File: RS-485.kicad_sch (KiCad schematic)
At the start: 15 parts, among them IC1 MAX485ESA+T

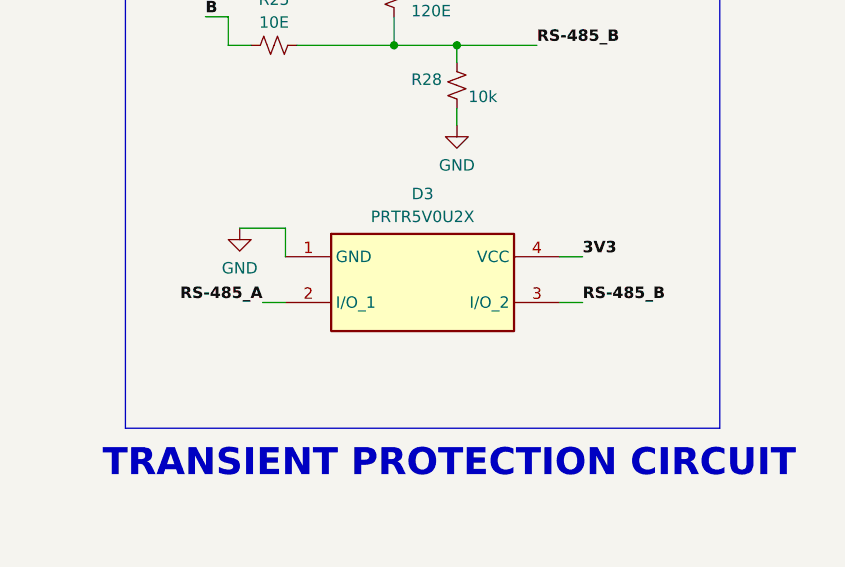
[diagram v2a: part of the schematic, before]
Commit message: Added IP5306 for power path management
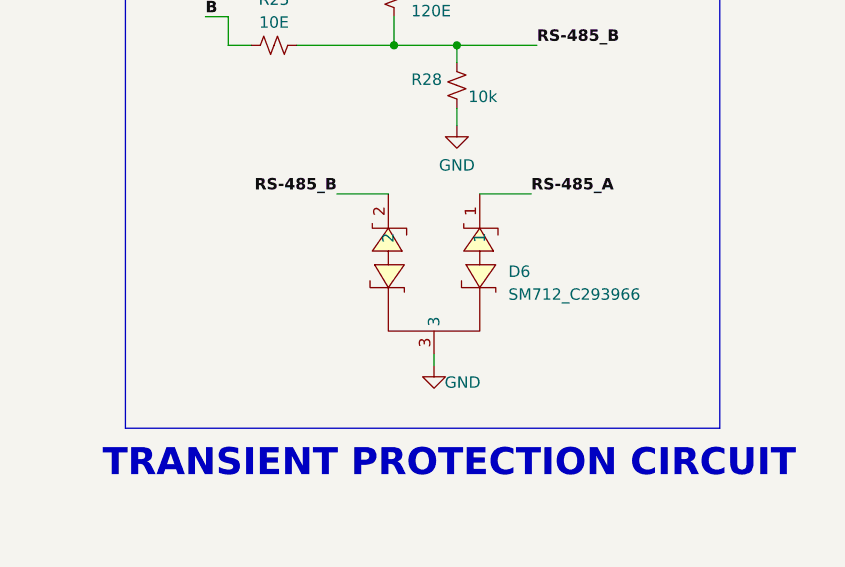
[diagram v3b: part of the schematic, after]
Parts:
- removed D3: PRTR5V0U2X, PRTR5V0U2X, symbol ESP32-S3_DB:PRTR5V0U2X
- added D6: SM712_C293966, easyeda2kicad:SOT-23_L2.9-W1.3-P1.90-LS2.4-BR, symbol ESP32-S3_DB:SM712_C293966
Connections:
- net GND: now also D6.3
- net RS_485_A: now also D6.1
- net RS_485_B: now also D6.2
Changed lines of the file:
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@@
+    (stroke (width 0) (type default))
+  )
+  (wire (pts (xy 234.95 106.68) (xy 229.235 106.68))
     (stroke (width 0) (type default))
   )
@@
     (stroke (width 0) (type default))
   )
-  (wire (pts (xy 256.54 113.665) (xy 254 113.665))
-    (stroke (width 0) (type default))
-  )
   (wire (pts (xy 125.095 108.585) (xy 125.095 111.76))
     (stroke (width 0) (type default))
@@
     (stroke (width 0) (type default))
   )
-  (wire (pts (xy 223.52 110.49) (xy 223.52 113.665))
-    (stroke (width 0) (type default))
-  )
   (wire (pts (xy 217.17 83.185) (xy 217.17 80.01))
     (stroke (width 0) (type default))
@@
     (stroke (width 0) (type default))
   )
-  (wire (pts (xy 220.98 118.745) (xy 223.52 118.745))
-    (stroke (width 0) (type default))
-  )
   (wire (pts (xy 62.865 102.235) (xy 60.96 102.235))
     (stroke (width 0) (type default))
@@
     (stroke (width 0) (type default))
   )
+  (wire (pts (xy 240.03 125.73) (xy 240.03 124.46))
+    (stroke (width 0) (type default))
+  )
   (wire (pts (xy 41.275 110.49) (xy 46.99 110.49))
     (stroke (width 0) (type default))
@@
     (stroke (width 0) (type default))
   )
-  (wire (pts (xy 218.44 110.49) (xy 223.52 110.49))
-    (stroke (width 0) (type default))
-  )
   (wire (pts (xy 235.585 86.995) (xy 235.585 90.17))
     (stroke (width 0) (type default))
@@
     (stroke (width 1) (type default) (color 72 72 72 1))
   )
-  (wire (pts (xy 256.54 118.745) (xy 254 118.745))
-    (stroke (width 0) (type default))
-  )
   (wire (pts (xy 235.585 90.17) (xy 242.57 90.17))
     (stroke (width 0) (type default))
@@
   )
   (wire (pts (xy 47.625 186.69) (xy 33.655 186.69))
+    (stroke (width 0) (type default))
+  )
+  (wire (pts (xy 250.825 106.68) (xy 245.11 106.68))
     (stroke (width 0) (type default))
   )
@@
     (effects (font (size 1.27 1.27) (thickness 0.254) bold (color 0 0 255 1)) (justify right bottom))
   )
-  (label "RS-485_A" (at 220.98 118.745 180) (fields_autoplaced)
-    (effects (font (size 1.27 1.27) (thickness 0.254) bold (color 0 0 0 1)) (justify right bottom))
+  (label "RS-485_A" (at 250.825 106.68 0) (fields_autoplaced)
+    (effects (font (size 1.27 1.27) (thickness 0.254) bold (color 0 0 0 1)) (justify left bottom))
   )
   (label "3V3" (at 47.625 165.735 180) (fields_autoplaced)
     (effects (font (size 1.27 1.27) (thickness 0.254) bold (color 255 0 0 1)) (justify right bottom))
   )
-  (label "3V3" (at 256.54 113.665 0) (fields_autoplaced)
-    (effects (font (size 1.27 1.27) (thickness 0.254) bold (color 255 0 0 1)) (justify left bottom))
-  )
   (label "RS-485_A" (at 47.625 181.61 180) (fields_autoplaced)
     (effects (font (size 1.27 1.27) (thickness 0.254) bold (color 0 0 0 1)) (justify right bottom))
@@
     (effects (font (size 1.27 1.27) (thickness 0.254) bold (color 0 0 255 1)) (justify right bottom))
   )
-  (label "RS-485_B" (at 256.54 118.745 0) (fields_autoplaced)
-    (effects (font (size 1.27 1.27) (thickness 0.254) bold (color 0 0 0 1)) (justify left bottom))
+  (label "RS-485_B" (at 229.235 106.68 180) (fields_autoplaced)
+    (effects (font (size 1.27 1.27) (thickness 0.254) bold (color 0 0 0 1)) (justify right bottom))
   )
   (hierarchical_label "485_TX" (shape output) (at 33.655 170.815 180) (fields_autoplaced)
@@
     )
   )
-  (symbol (lib_id "ESP32-S3_DB:PRTR5V0U2X") (at 223.52 113.665 0) (unit 1)
-    (in_bom yes) (on_board yes) (dnp no) (fields_autoplaced)
-    (property "Reference" "D3" (at 238.76 106.68 0)
-      (effects (font (size 1.27 1.27)))
-    )
-    (property "Value" "PRTR5V0U2X" (at 238.76 109.22 0)
-      (effects (font (size 1.27 1.27)))
-    )
-    (property "Footprint" "PRTR5V0U2X" (at 250.19 208.585 0)
-      (effects (font (size 1.27 1.27)) (justify left top) hide)
-    )
-    (property "Datasheet" "https://assets.nexperia.com/documents/data-sheet/PRTR5V0U2X.pdf" (at 250.19 308.585 0)
-      (effects (font (size 1.27 1.27)) (justify left top) hide)
-    )
-    (property "Height" "1.1" (at 250.19 508.585 0)
-      (effects (font (size 1.27 1.27)) (justify left top) hide)
-    )
-    (property "Manufacturer_Name" "Nexperia" (at 250.19 608.585 0)
-      (effects (font (size 1.27 1.27)) (justify left top) hide)
-    )
-    (property "Manufacturer_Part_Number" "PRTR5V0U2X" (at 250.19 708.585 0)
-      (effects (font (size 1.27 1.27)) (justify left top) hide)
-    )
-    (property "Mouser Part Number" "N/A" (at 250.19 808.585 0)
-      (effects (font (size 1.27 1.27)) (justify left top) hide)
-    )
-    (property "Mouser Price/Stock" "https://www.mouser.co.uk/ProductDetail/Nexperia/PRTR5V0U2X?qs=vHuUswq2%252BsxqVTVM0kNyWw%3D%3D" (at 250.19 908.585 0)
-      (effects (font (size 1.27 1.27)) (justify left top) hide)
-    )
-    (property "Arrow Part Number" "" (at 250.19 1008.585 0)
-      (effects (font (size 1.27 1.27)) (justify left top) hide)
-    )
-    (property "Arrow Price/Stock" "" (at 250.19 1108.585 0)
-      (effects (font (size 1.27 1.27)) (justify left top) hide)
-    )
-    (pin "1")
-    (pin "2")
-    (pin "3")
-    (pin "4")
-    (instances
-      (project "ESP32-S3_DB"
-        (path "/b7fc4bd3-c219-4455-832b-8d795385dcf1/9b4afe2f-79e5-4a56-98d7-d16b193c0e70"
-          (reference "D3") (unit 1)
-        )
-      )
-    )
-  )
   (symbol (lib_id "ESP32-S3_DB:R_Small_US") (at 222.25 90.17 90) (unit 1)
     (in_bom yes) (on_board yes) (dnp no) (fields_autoplaced)
@@
     )
   )
-  (symbol (lib_id "ESP32-S3_DB:GND") (at 218.44 110.49 0) (unit 1)
+  (symbol (lib_id "ESP32-S3_DB:GND") (at 240.03 125.73 0) (unit 1)
+    (in_bom yes) (on_board yes) (dnp no)
+    (property "Reference" "#PWR037" (at 240.03 132.08 0)
+      (effects (font (size 1.27 1.27)) hide)
+    )
+    (property "Value" "GND" (at 243.205 127.635 0)
+      (effects (font (size 1.27 1.27)))
+    )
+    (property "Footprint" "" (at 240.03 125.73 0)
+      (effects (font (size 1.27 1.27)) hide)
+    )
+    (property "Datasheet" "" (at 240.03 125.73 0)
+      (effects (font (size 1.27 1.27)) hide)
+    )
+    (pin "1")
+    (instances
+      (project "ESP32-S3_DB"
+        (path "/b7fc4bd3-c219-4455-832b-8d795385dcf1/9b4afe2f-79e5-4a56-98d7-d16b193c0e70"
+          (reference "#PWR037") (unit 1)
+        )
+      )
+    )
+  )
+  (symbol (lib_id "ESP32-S3_DB:SM712_C293966") (at 240.03 114.3 180) (unit 1)
     (in_bom yes) (on_board yes) (dnp no) (fields_autoplaced)
-    (property "Reference" "#PWR037" (at 218.44 116.84 0)
-      (effects (font (size 1.27 1.27)) hide)
-    )
-    (property "Value" "GND" (at 218.44 114.935 0)
-      (effects (font (size 1.27 1.27)))
-    )
-    (property "Footprint" "" (at 218.44 110.49 0)
-      (effects (font (size 1.27 1.27)) hide)
-    )
-    (property "Datasheet" "" (at 218.44 110.49 0)
-      (effects (font (size 1.27 1.27)) hide)
-    )
-    (pin "1")
-    (instances
-      (project "ESP32-S3_DB"
-        (path "/b7fc4bd3-c219-4455-832b-8d795385dcf1/9b4afe2f-79e5-4a56-98d7-d16b193c0e70"
-          (reference "#PWR037") (unit 1)
-        )
-      )
+    (property "Reference" "D6" (at 248.285 115.315 0)
+      (effects (font (size 1.27 1.27)) (justify right))
+    )
+    (property "Value" "SM712_C293966" (at 248.285 117.855 0)
+      (effects (font (size 1.27 1.27)) (justify right))
+    )
+    (property "Footprint" "easyeda2kicad:SOT-23_L2.9-W1.3-P1.90-LS2.4-BR" (at 240.03 99.06 0)
+      (effects (font (size 1.27 1.27)) hide)
+    )
+    (property "Datasheet" "https://lcsc.com/product-detail/TVS_DOWO-SM712_C293966.html" (at 240.03 96.52 0)
+      (effects (font (size 1.27 1.27)) hide)
+    )
+    (property "LCSC Part" "C293966" (at 240.03 93.98 0)
+      (effects (font (size 1.27 1.27)) hide)
+    )
+    (pin "1")
+    (pin "2")
+    (pin "3")
+    (instances
+      (project "ESP32-S3_DB"
+        (path "/b7fc4bd3-c219-4455-832b-8d795385dcf1/9b4afe2f-79e5-4a56-98d7-d16b193c0e70"
+          (reference "D6") (unit 1)
+        )
+      )

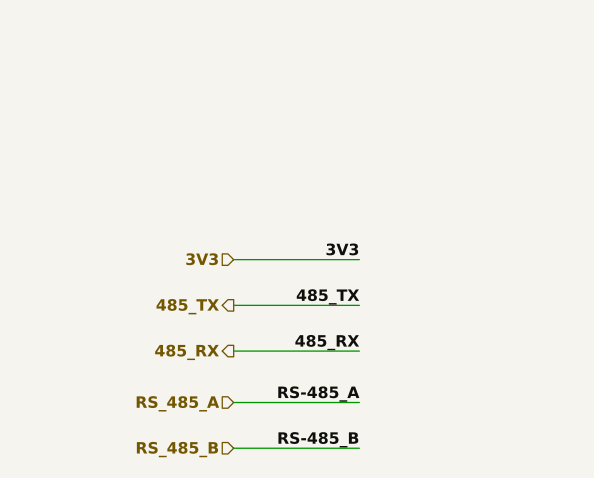
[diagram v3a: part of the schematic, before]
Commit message: Assigned UART port 2 for RS-485
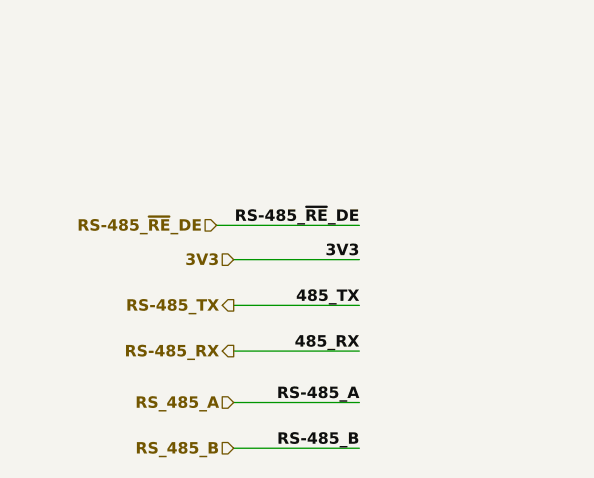
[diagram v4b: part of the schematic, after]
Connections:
- net 485_RX renamed RS-485_RX
- net 485_TX renamed RS-485_TX
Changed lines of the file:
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@@
+    (stroke (width 0) (type default))
+  )
+  (wire (pts (xy 47.625 161.925) (xy 31.75 161.925))
     (stroke (width 0) (type default))
   )
@@
   )
   (label "RS-485_~{RE}_DE" (at 110.49 96.52 0) (fields_autoplaced)
-    (effects (font (size 1.27 1.27) bold (color 0 132 132 1)) (justify left bottom))
+    (effects (font (size 1.27 1.27) bold (color 0 194 0 1)) (justify left bottom))
   )
   (label "B" (at 214.63 86.995 0) (fields_autoplaced)
@@
     (effects (font (size 1.27 1.27) (thickness 0.254) bold (color 0 0 0 1)) (justify right bottom))
   )
+  (label "RS-485_~{RE}_DE" (at 47.625 161.925 180) (fields_autoplaced)
+    (effects (font (size 1.27 1.27) bold (color 0 194 0 1)) (justify right bottom))
+  )
   (label "3V3" (at 247.015 71.12 180) (fields_autoplaced)
     (effects (font (size 1.27 1.27) (thickness 0.254) bold (color 255 0 0 1)) (justify right bottom))
@@
     (effects (font (size 1.27 1.27) (thickness 0.254) bold (color 0 0 0 1)) (justify right bottom))
   )
-  (hierarchical_label "485_TX" (shape output) (at 33.655 170.815 180) (fields_autoplaced)
+  (hierarchical_label "RS-485_TX" (shape output) (at 33.655 170.815 180) (fields_autoplaced)
     (effects (font (size 1.27 1.27) bold (color 0 0 255 1)) (justify right))
   )
@@
     (effects (font (size 1.27 1.27) (thickness 0.254) bold (color 255 0 0 1)) (justify right))
   )
-  (hierarchical_label "485_RX" (shape output) (at 33.655 175.895 180) (fields_autoplaced)
+  (hierarchical_label "RS-485_RX" (shape output) (at 33.655 175.895 180) (fields_autoplaced)
     (effects (font (size 1.27 1.27) bold (color 0 0 255 1)) (justify right))
   )
+  (hierarchical_label "RS-485_~{RE}_DE" (shape input) (at 31.75 161.925 180) (fields_autoplaced)
+    (effects (font (size 1.27 1.27) bold (color 0 194 0 1)) (justify right))
+  )
   (hierarchical_label "RS_485_B" (shape input) (at 33.655 186.69 180) (fields_autoplaced)

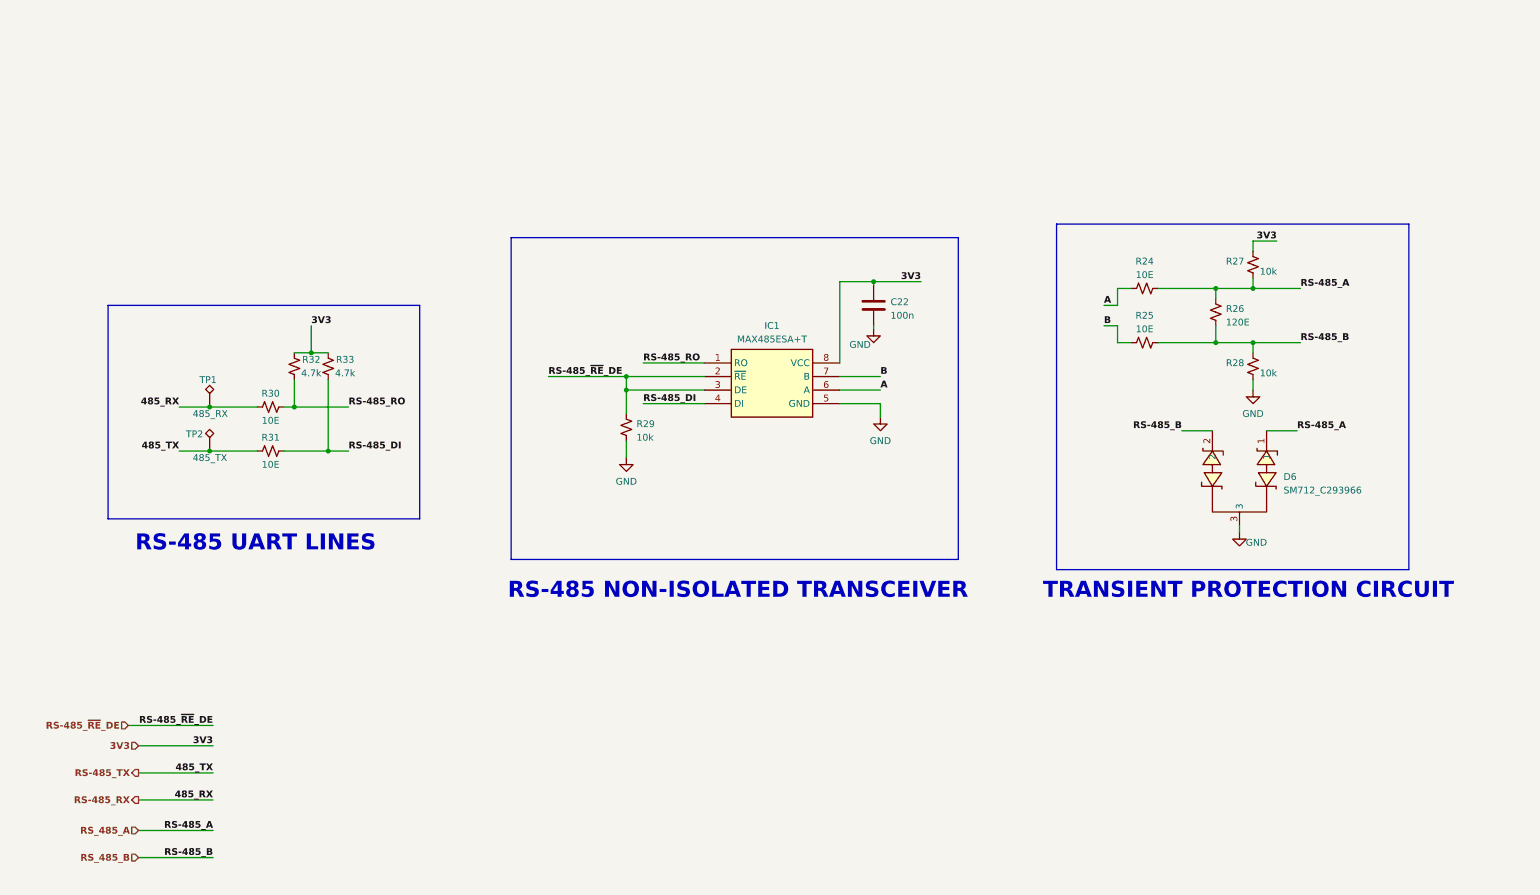
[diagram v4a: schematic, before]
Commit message: Added Female Headers
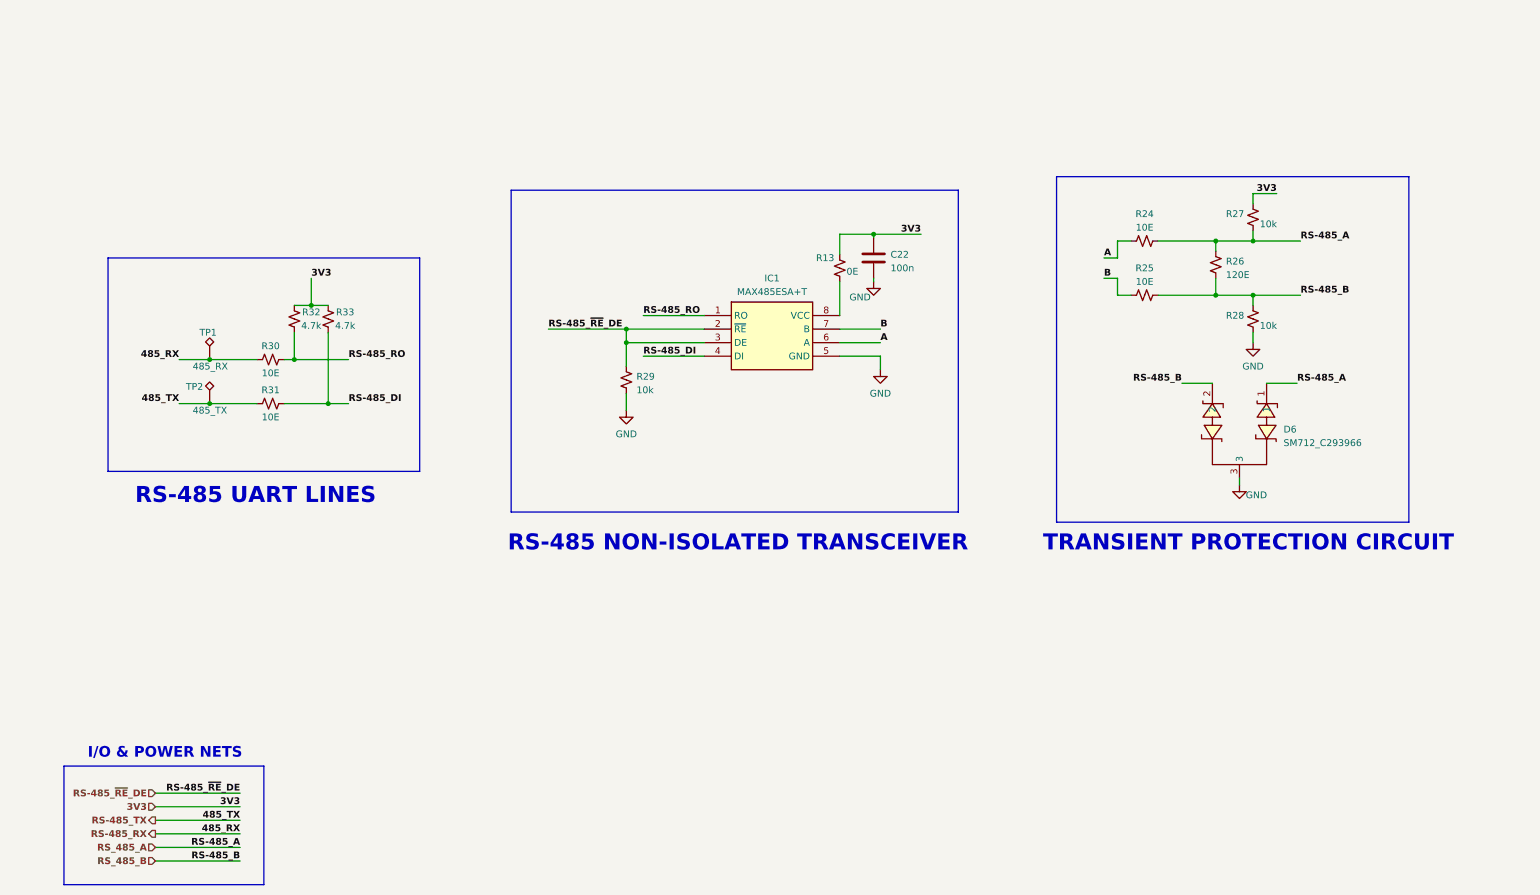
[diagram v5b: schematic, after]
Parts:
- added R13: 0E, symbol ESP32-S3_DB:R_Small_US
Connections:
- net 3V3: now also R13.1; no longer IC1.8 (VCC)
- new net: IC1.8 (VCC), R13.2
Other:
- note added: "I/O & POWER NETS"
- moved on the sheet: C22, D6, IC1, R24, R25, R26, R27, R28, R29, R30, R31, R32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

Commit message: Assigned PN and Footprint for C
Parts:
- C22: value 100n -> 100nF; footprint (none) -> ESP32-S3_DB:C_0402_1005Metric; PN (none) -> EMK107B7104KAHT
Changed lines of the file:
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@@
       (effects (font (size 1.27 1.27)) (justify left))
     )
-    (property "Value" "100n" (at 174.625 76.2 0)
+    (property "Value" "100nF" (at 174.625 76.2 0)
       (effects (font (size 1.27 1.27)) (justify left))
     )
-    (property "Footprint" "" (at 172.4152 78.105 0)
+    (property "Footprint" "ESP32-S3_DB:C_0402_1005Metric" (at 172.4152 78.105 0)
       (effects (font (size 1.27 1.27)) hide)
     )
@@
       (effects (font (size 1.27 1.27)) hide)
     )
+    (property "PN" "EMK107B7104KAHT" (at 171.45 74.295 0)
+      (effects (font (size 1.27 1.27)) hide)
+    )
